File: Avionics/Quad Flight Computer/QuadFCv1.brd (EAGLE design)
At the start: 76.2 x 50.2 mm, 86 parts, among them J1 10104111_MICROUSBAB, SW1 2-1437565-9, U1 74LVC4245APW, U10 ATMEGA32U2-MU, U2 TM4C123GH6PZ, U3 MPU-6050-1, U4 HMC5883LSMD, U8 SPI_PPM, X3 HWB, Y1 32.768KHZ, Y2 AWSCR-20.00CW-T, Y3 PRQC16.00SR5010X000

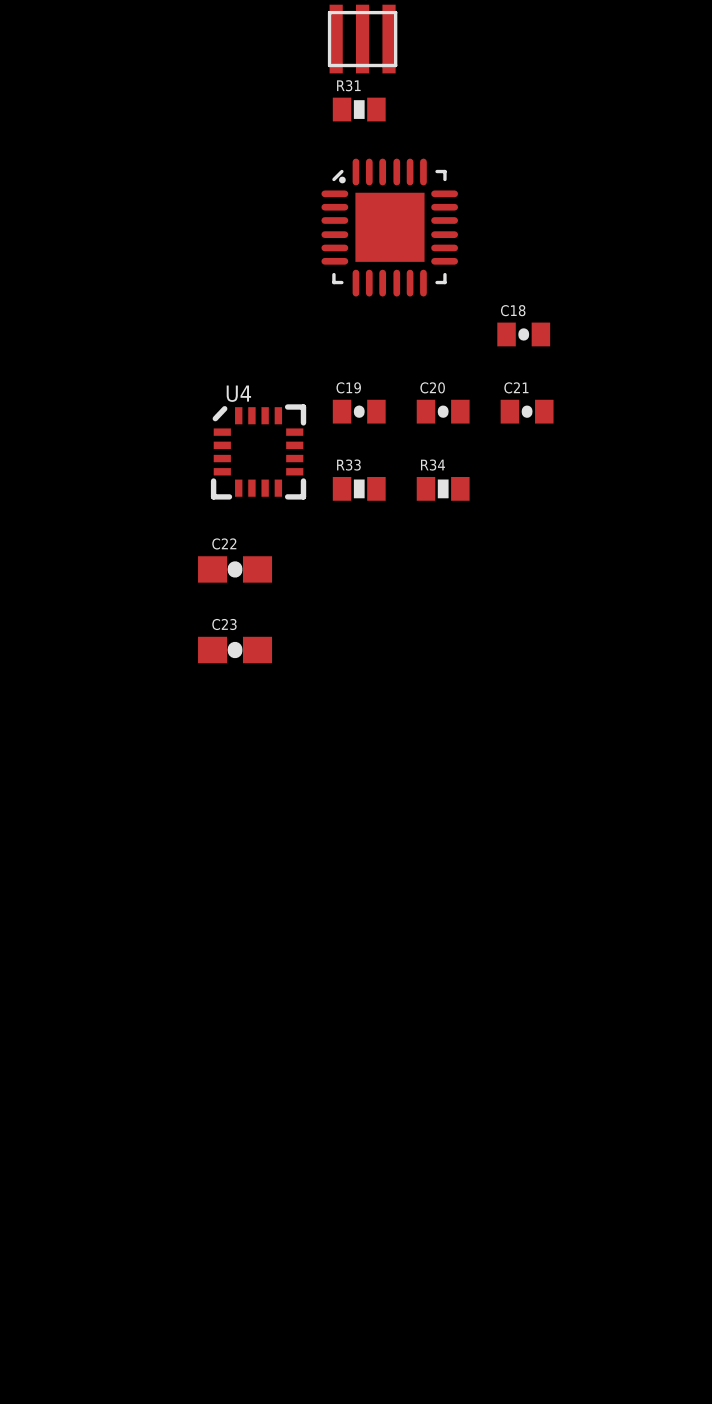
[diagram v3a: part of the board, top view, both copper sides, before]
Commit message: Exported all parts to libraries. Replaced IMU with MPU-6000.
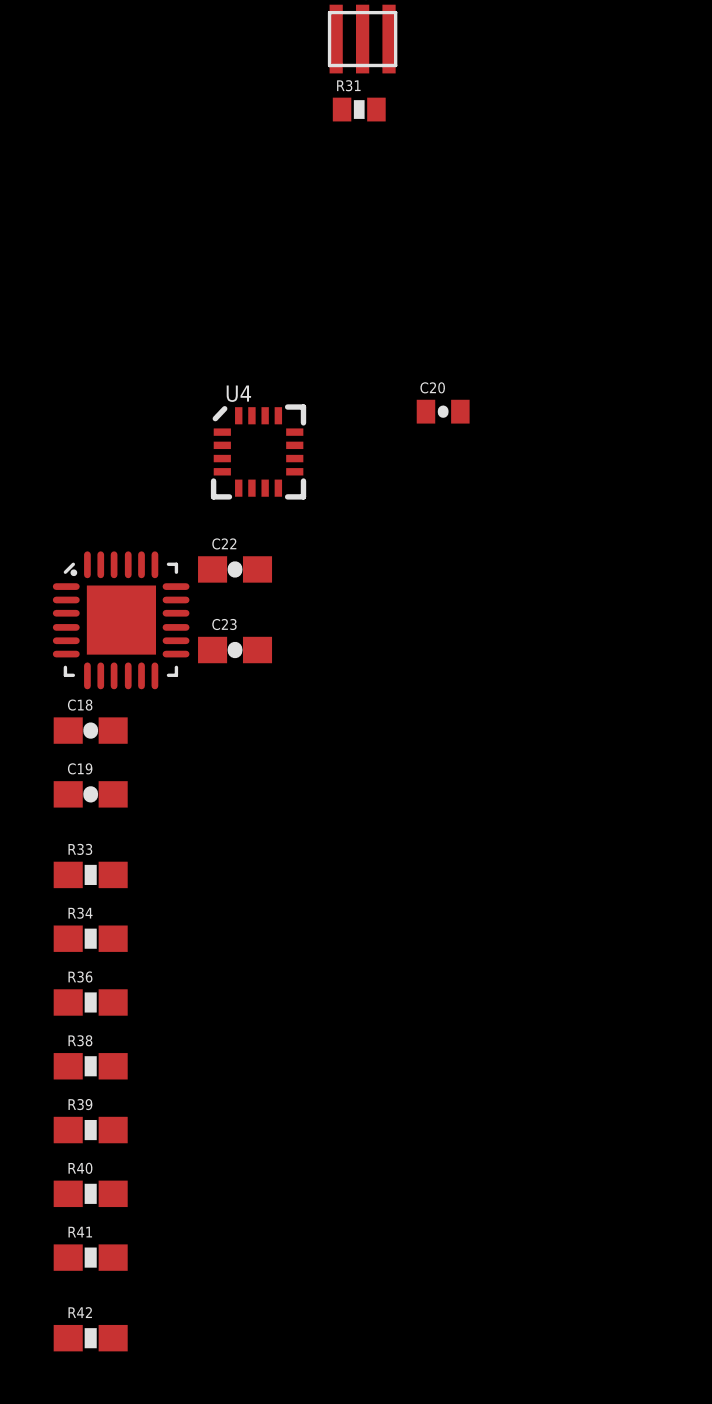
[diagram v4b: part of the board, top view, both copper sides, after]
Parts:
- removed C21: 10nF, SparkFun:0402-CAP
- removed U3: MPU-6050-1, Testing:QFN-24-4MM2
- added R36, R39, R40, R42: DNP, SparkFun-Resistors:0603-RES
- added R38, R41: 0, SparkFun-Resistors:0603-RES
- added U5: MPU-6000, Invesense:QFN-24-4MM2
- C18, C19: device SparkFun:0402-CAP -> SparkFun-Capacitors:0603-CAP
- R33, R34: value 10k -> 0; device SparkFun:0402-RES -> SparkFun-Resistors:0603-RES
- moved C18 22.2 mm to (-28.4, -177.3)
- moved R34 21.6 mm to (-28.4, -185.2)
- moved R33 17.8 mm to (-28.4, -182.8)
- moved C19 17.7 mm to (-28.4, -179.7)
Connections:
- removed net IMU_INT: U3.12
- removed net VIO: C21.1, U3.8
- new net FC_IMU_INT: U5.12
- new net FC_IMU_SPI_CS: R41.2
- new net FC_IMU_SPI_MISO: R38.1
- new net FC_IMU_SPI_MOSI: R34.2
- new net FC_IMU_SPI_SCLK: R33.2
- new net N$38: R33.1, R39.2, U5.23
- new net N$39: R34.1, R40.2, U5.24
- new net N$40: R41.1, U5.8
- new net N$41: R36.2, R38.2, R42.1, U5.9
- net 3.3V: now also R42.2, U5.13; no longer R33.2, R34.2, U3.13
- net AUX_SCL: now also U5.7; no longer U3.7
- net AUX_SDA: now also U5.6; no longer U3.6
- net FC_IMU_SCL: now also R39.1; no longer R33.1, U3.23
- net FC_IMU_SDA: now also R40.1; no longer R34.1, U3.24
- net GND: now also R36.1, U5.1, U5.11, U5.18; no longer C21.2, U3.1, U3.11, U3.18, U3.9
- net N$33: now also U5.20; no longer U3.20
- net N$34: now also U5.10; no longer U3.10

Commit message: Connected sensor network and added pressure sensor
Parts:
- removed R36, R42: DNP, SparkFun-Resistors:0603-RES
- removed R38, R41: 0, SparkFun-Resistors:0603-RES
- added C21: 0.1uF, SparkFun-Capacitors:0603-CAP
- added U6: MS5611-01BA, 3DRobotics:MS5611-01BA
- moved R33 30.5 mm to (-28.4, -213.2)
- moved R34 30.5 mm to (-28.4, -215.6)
- moved SW1 1.53 mm to (18.2, 34.5)
- moved J1 0.28 mm to (27.1, 4.83)
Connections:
- net PPM_STATUS0 renamed FC_PPM_STATUS0
- net PPM_STATUS1 renamed FC_PPM_STATUS1
- removed net FC_IMU_SCL: R39.1, U2.62, U4.1
- removed net FC_IMU_SDA: R40.1, U2.61, U4.16
- removed net FC_IMU_SPI_CS: R41.2
- removed net FC_IMU_SPI_MISO: R38.1
- removed net FC_IMU_SPI_MOSI: R34.2
- removed net FC_IMU_SPI_SCLK: R33.2
- removed net FC_SSI3CLK: U2.49
- removed net FC_SSI3FSS: U2.48
- removed net FC_SSI3RX: U2.47
- removed net FC_SSI3TX: U2.46
- removed net N$38: R33.1, R39.2, U5.23
- removed net N$39: R34.1, R40.2, U5.24
- removed net N$40: R41.1, U5.8
- removed net N$41: R36.2, R38.2, R42.1, U5.9
- new net FC_IMU_CS_L: U2.48, U5.8
- new net FC_IMU_MISO: U2.47, U5.9
- new net FC_IMU_MOSI: U2.46, U5.24
- new net FC_IMU_SCLK: U2.49, U5.23
- new net FC_PPM_IN: R28.1
- new net FC_SENSE_SCL: R33.2, U2.62, U6.8
- new net FC_SENSE_SDA: R34.2, U2.61, U6.7
- new net FC_USB_STATUS: R31.1
- new net MAG_SCL: R33.1, R39.1, U4.1
- new net MAG_SDA: R34.1, R40.1, U4.16
- net 3.3V: now also C21.1, U6.1, U6.2; no longer R42.2
- net AUX_SCL: now also R39.2
- net AUX_SDA: now also R40.2
- net GND: now also C21.2, U6.3, U6.5; no longer R36.1

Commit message: Added 16MB flash chip for core event logging and mission profile configuration. Internal EEPROM will be used for core configuration (failsafe modes, dead zones, etc), external flash will store mission parameters and user settings.
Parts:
- removed R46, R47, R51: 1k, SparkFun:0402-RES
- added R36: 1k, SparkFun:0402-RES
- added R38: DNP, SparkFun-Resistors:0603-RES
- added R41: 0, SparkFun-Resistors:0603-RES
- added U7: MS5611-01BA, 3DRobotics:MS5611-01BA
- added U9: S25FL127S, Shared Libraries:SOIC8
- C1: value 1uF -> 0.1uF; device SparkFun-Passives:0603-CAP -> SparkFun-Capacitors:0603-CAP
- C12: value 18pF -> 1uF
- C14: value .1uF -> 1uF; device SparkFun:0402-CAP -> SparkFun-Passives:0603-CAP
- C15: value 0.1uF -> .1uF; device SparkFun-Capacitors:0603-CAP -> SparkFun:0402-CAP
- C16: value .1uF -> 1uF
- C17: value 1uF -> .1uF
- C18: device SparkFun-Capacitors:0603-CAP -> SparkFun:0402-CAP
- C19: value 2.2nF -> 0.1uF
- C2, C3: value 1uF -> 0.1uF
- C20: value 0.1uF -> 2.2nF; device SparkFun:0402-CAP -> SparkFun-Capacitors:0603-CAP
- C21: value 0.1uF -> 4.7uF
- C23: value 4.7uF -> 0.1uF
- C7: value 0.1uF -> 18pF
- C9: value 0.1uF -> 1uF
- R13: value 0 -> 220; device SparkFun-Resistors:0805 -> SparkFun-Resistors:0603-RES
- R22: value 10K -> 220
- R23: value 49.9K -> 220
- R24: value 22 -> 220; device Shared Libraries:0603-RES -> SparkFun-Resistors:0603-RES
- R25: value 22-DNP -> 220; device Shared Libraries:0603-RES -> SparkFun-Resistors:0603-RES
- R26: value 22-DNP -> 49.9K; device Shared Libraries:0603-RES -> SparkFun-Resistors:0603-RES
- R27: value 0 -> 10K; device Shared Libraries:0603-RES -> SparkFun-Resistors:0603-RES
- R28: value 1K -> 1M
- R29: value 1M -> 10K
- R3: value 22 -> 22-DNP
- R31: value 1k -> 1K
- R33, R34: value 0 -> 1k; device SparkFun-Resistors:0603-RES -> SparkFun:0402-RES
- R37: value 10K -> 1k
- R4: value 0 -> 22; device SparkFun-Resistors:0805 -> Shared Libraries:0603-RES
- R40: value DNP -> 0
- R5: value 220 -> 22-DNP; device SparkFun-Resistors:0603-RES -> Shared Libraries:0603-RES
- R6: value 220 -> 0; device SparkFun-Resistors:0603-RES -> Shared Libraries:0603-RES
- R7: value 220 -> 22; device SparkFun-Resistors:0603-RES -> Shared Libraries:0603-RES
- R8, R9: value 220 -> 0; device SparkFun-Resistors:0603-RES -> SparkFun-Resistors:0805
- U1: value 74LVC4245APW -> TM4C123GH6PZ; device Shared Libraries:TSSOP24 -> Shared Libraries:LQFP100
- U2: value TM4C123GH6PZ -> 74LVC4245APW; device Shared Libraries:LQFP100 -> Shared Libraries:TSSOP24
- U4: value HMC5883LSMD -> SPI_PPM; device Shared Libraries:16LPCC -> SparkFunv2:2X3-NS
- U6: value MS5611-01BA -> HMC5883LSMD; device 3DRobotics:MS5611-01BA -> Shared Libraries:16LPCC
- U8: value SPI_PPM -> 74AUP1G19GW; device SparkFunv2:2X3-NS -> Shared Libraries:SOT363_PHILIPS
- moved C15 173.3 mm to (-4.95, -135.8), turned to 0 degrees
- moved C14 139.3 mm to (13.3, 1.91)
- moved C7 129.2 mm to (36.8, 26.0), turned to 270 degrees
- moved C4 128.6 mm to (39.4, 31.8), turned to 270 degrees
- moved C12 114.5 mm to (-18.4, -77.5), turned to 0 degrees
- moved U8 111.7 mm to (-28.3, -220.5)
- moved C1 106.4 mm to (-18.4, -99.7)
- moved R34 77.6 mm to (-15.1, -139.2)
- moved R33 77.5 mm to (-5.59, -139.2)
- moved JP1 73.3 mm to (73.0, 8.26), turned to 90 degrees
- moved JP2 73.3 mm to (3.81, 32.4), turned to 270 degrees
- moved R21 62.2 mm to (7.62, 19.7), turned to 180 degrees
- moved R12 62.1 mm to (69.2, 19.1), turned to 0 degrees
- moved R8 61.9 mm to (69.2, 13.3)
- moved R20 61.8 mm to (7.62, 21.8), turned to 180 degrees
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- renumbered F2 to F1, LED4 to LED2, LED5 to LED1, LED7 to LED3, U10 to U3, X3 to X1
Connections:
- removed net FC_SSI0CLK: U2.28
- removed net FC_SSI0FSS: U2.29
- removed net FC_SSI0RX: U2.30
- removed net FC_SSI0TX: U2.31
- new net FC_MEM_CLK: U1.28, U9.6
- new net FC_MEM_FSS: U1.29, U8.3
- new net FC_MEM_MISO: U1.30, U9.2
- new net FC_MEM_MOSI: U1.31, U9.5
- new net FC_MEM_SEL: U8.1
- new net FLASH_CS_L: U8.6, U9.1
- new net SD_CS_L: U8.4
- net 3.3V: now also C1.1, C13.1, C18.1, C2.1, C23.1, R26.2, U1.20, U1.32, U1.44, U1.5, U1.55, U1.56, U1.67, U1.7, U1.80, U1.93, U2.23, U2.24, U6.13, U6.4, U7.1, U7.2, U8.5, U9.8; no longer C20.1, C21.1, C4.1, C7.1, C9.1, R23.2, U1.23, U1.24, U2.20, U2.32, U2.44, U2.5, U2.55, U2.56, U2.67, U2.7, U2.80, U2.93, U4.13, U4.2, U4.4, U6.1
- net 5V: now also C15.1, C17.1, R29.2, R33.1, R34.1, R8.2, R9.2, U2.1, U4.2; no longer C14.1, C16.1, R13.2, R32.1, R37.2, R4.2, R51.1, U1.1, U8.2
- net AUX_SCL: now also R38.2; no longer R39.2
- net AUX_SDA: now also R39.2; no longer R40.2
- net FC_AIN0: now also U1.12; no longer U2.12
- net FC_AIN1: now also U1.13; no longer U2.13
- net FC_AIN20: now also U1.90; no longer U2.90
- net FC_AIN21: now also U1.89; no longer U2.89
- net FC_AIN4: now also U1.100; no longer U2.100
- net FC_AIN5: now also U1.99; no longer U2.99
- net FC_IMU_CS_L: now also U1.48; no longer U2.48
- net FC_IMU_MISO: now also U1.47; no longer U2.47
- net FC_IMU_MOSI: now also U1.46; no longer U2.46
- net FC_IMU_SCLK: now also U1.49; no longer U2.49
- net FC_JTAG_TCK: now also U1.85; no longer U2.85
- net FC_JTAG_TDI: now also U1.83; no longer U2.83
- net FC_JTAG_TDO: now also U1.82; no longer U2.82
- net FC_JTAG_TMS: now also U1.84; no longer U2.84
- net FC_MAG_DRDY_L: now also U6.15; no longer U4.15
- net FC_PA6: now also U1.34; no longer U2.34
- net FC_PA7: now also U1.35; no longer U2.35
- net FC_PB2: now also U1.72; no longer U2.72
- net FC_PB3: now also U1.73; no longer U2.73
- net FC_PB4: now also U1.92; no longer U2.92
- net FC_PB5: now also U1.91; no longer U2.91
- net FC_PD0: now also U1.1; no longer U2.1
- net FC_PD1: now also U1.2; no longer U2.2
- net FC_PD2: now also U1.3; no longer U2.3
- net FC_PD3: now also U1.4; no longer U2.4
- net FC_PD4: now also U1.97; no longer U2.97
- net FC_PD5: now also U1.98; no longer U2.98
- net FC_PE4: now also U1.95; no longer U2.95
- net FC_PE5: now also U1.96; no longer U2.96
- net FC_PF0: now also U1.40; no longer U2.40
- net FC_PF1: now also U1.41; no longer U2.41
- net FC_PF2: now also U1.42; no longer U2.42
- net FC_PF3: now also U1.43; no longer U2.43
- net FC_PF4: now also U1.39; no longer U2.39
- net FC_PF5: now also U1.37; no longer U2.37
- net FC_PF6: now also U1.36; no longer U2.36
- net FC_PF7: now also U1.58; no longer U2.58
- net FC_PG2: now also U1.60; no longer U2.60
- net FC_PG3: now also U1.59; no longer U2.59
- net FC_PG4: now also U1.74; no longer U2.74
- net FC_PG5: now also U1.75; no longer U2.75
- net FC_PG6: now also U1.87; no longer U2.87
- net FC_PG7: now also U1.88; no longer U2.88
- net FC_PJ2: now also U1.11; no longer U2.11
- net FC_PPM_IN: now also R31.1; no longer R28.1
- net FC_PPM_STATUS0: now also R37.1; no longer R47.1
- net FC_PPM_STATUS1: now also R32.1; no longer R46.1
- net FC_PWMOUT1: now also U1.16, U2.21; no longer U1.21, U2.16
- net FC_PWMOUT2: now also U1.17, U2.20; no longer U1.20, U2.17
- net FC_PWMOUT3: now also U1.18, U2.19; no longer U1.19, U2.18
- net FC_PWMOUT4: now also U1.19, U2.18; no longer U1.18, U2.19
- net FC_PWMOUT5: now also U1.79, U2.17; no longer U1.17, U2.79
- net FC_PWMOUT6: now also U1.78, U2.16; no longer U1.16, U2.78
- net FC_PWMOUT7: now also U1.77, U2.15; no longer U1.15, U2.77
- net FC_PWMOUT8: now also U1.76, U2.14; no longer U1.14, U2.76
- net FC_PWMOUT_ARM_L: now also R26.1, U2.22; no longer R23.1, U1.22
- net FC_RESET_L: now also C4.1, U1.63; no longer C15.1, U2.63
- net FC_SENSE_SCL: now also R41.2, U1.62, U7.8; no longer R33.2, U2.62, U6.8
- net FC_SENSE_SDA: now also R40.2, U1.61, U7.7; no longer R34.2, U2.61, U6.7
- net FC_U0RX: now also U1.26; no longer U2.26
- net FC_U0TX: now also U1.27; no longer U2.27
- net FC_U1RX: now also U1.25; no longer U2.25
- net FC_U1TX: now also U1.24; no longer U2.24
- net FC_U3RX: now also U1.23; no longer U2.23
- net FC_U3TX: now also U1.22; no longer U2.22
- net FC_U7RX: now also U1.15; no longer U2.15
- net FC_U7TX: now also U1.14; no longer U2.14
- net FC_USB0DM: now also R7.1, U1.68; no longer R3.1, U2.68
- net FC_USB0DP: now also R4.1, U1.69; no longer R24.1, U2.69
- net FC_USB0ID: now also R6.1, U1.70; no longer R27.1, U2.70
- net FC_USB0VBUS: now also U1.71; no longer U2.71
- net FC_USB_STATUS: now also R36.1; no longer R31.1
- net GND: now also C1.2, C12.2, C14.1, R27.1, U1.10, U1.21, U1.33, U1.45, U1.57, U1.6, U1.64, U1.81, U1.9, U1.94, U2.11, U2.12, U2.13, U4.6, U6.11, U6.9, U7.3, U7.5, U8.2, U9.4; no longer C1.1, C14.2, C7.2, R22.1, U1.11, U1.12, U1.13, U2.10, U2.21, U2.33, U2.45, U2.57, U2.6, U2.64, U2.81, U2.9, U2.94, U4.11, U4.9, U6.3, U6.5, U8.6
- net GNDX: now also C7.2, U1.53; no longer C12.2, U2.53
- net MAG_SCL: now also R38.1, R41.1, U6.1; no longer R33.1, R39.1, U4.1
- net MAG_SDA: now also R39.1, U6.16; no longer R34.1, U4.16
- net N$1: now also JP2.3, R18.2; no longer JP1.3, R5.2
- net N$10: now also JP1.4, R11.2; no longer JP2.4, R15.2
- net N$11: now also JP1.5, R12.2; no longer JP2.5, R16.2
- net N$12: now also JP1.6, R13.2; no longer JP2.6, R17.2
- net N$13: now also JP1.7, R14.2; no longer JP2.7, R18.2
- net N$14: now also JP1.8, R15.2; no longer JP2.8, R19.2
- net N$15: now also JP1.9, R16.2; no longer JP2.9, R20.2
- net N$16: now also JP1.10, R17.2; no longer JP2.10, R21.2
- net N$17: now also C14.2, U1.8; no longer C1.2, U2.8
- net N$18: now also C12.1, C9.1, U1.38, U1.86; no longer C13.1, C2.1, U2.38, U2.86
- net N$19: now also C11.1, U1.54; no longer C12.1, U2.54
- net N$2: now also JP2.4, R19.2; no longer JP1.4, R6.2
- net N$20: now also R27.2, U2.2; no longer R22.2, U1.2
- net N$21: now also C7.1, U1.52; no longer C11.1, U2.52
- net N$22: now also U1.50; no longer U2.50
- net N$23: now also JP2.2, R9.1; no longer JP1.2, R4.1
- net N$24: now also U1.65; no longer U2.65
- net N$25: now also U1.66; no longer U2.66
- net N$26: now also JP1.2, R8.1; no longer JP2.2, R13.1
- net N$27: now also R6.2; no longer R27.2
- net N$28: now also R7.2; no longer R26.2
- net N$29: now also R4.2, R5.2; no longer R24.2, R25.2
- net N$3: now also JP2.5, R20.2; no longer JP1.5, R7.2
- net N$30: now also R33.2; no longer R35.2
- net N$31: now also R34.2; no longer R32.2
- net N$32: now also R35.2; no longer R51.2
- net N$33: now also C20.1; no longer C19.1
- net N$34: now also C19.1; no longer C18.1
- net N$35: now also C21.1, U6.10; no longer C23.1, U4.10
- net N$36: now also U6.8; no longer U4.8
- net N$37: now also U6.12; no longer U4.12
- net N$4: now also JP2.6, R21.2; no longer JP1.6, R8.2
- net N$5: now also JP2.7, R22.2; no longer JP1.7, R9.2
- net N$6: now also JP2.8, R23.2; no longer JP1.8, R10.2
- net N$7: now also JP2.9, R24.2; no longer JP1.9, R11.2
- net N$8: now also JP2.10, R25.2; no longer JP1.10, R12.2
- net N$9: now also JP1.3, R10.2; no longer JP2.3, R14.2
- net PPM_OUT: now also R31.2; no longer R28.2
- net PPM_PD0: now also R37.2; no longer R47.2
- net PPM_PD1: now also R32.2; no longer R46.2
- net PPM_RST: now also R29.1, U4.5; no longer R37.1, U8.5
- net PPM_USBDM: now also R3.1; no longer R26.1
- net PPM_USBDP: now also R5.1; no longer R25.1
- net PPM_USB_STATUS: now also R36.2; no longer R31.2
- net PWMIN1: now also R18.1; no longer R5.1
- net PWMIN2: now also R19.1, U4.3; no longer R6.1, U8.3
- net PWMIN3: now also R20.1, U4.4; no longer R7.1, U8.4
- net PWMIN4: now also R21.1, U4.1; no longer R8.1, U8.1
- net PWMIN5: now also R22.1; no longer R9.1
- net PWMIN6: now also R23.1; no longer R10.1
- net PWMIN7: now also R24.1; no longer R11.1
- net PWMIN8: now also R25.1; no longer R12.1
- net PWMOUT1: now also R10.1, U2.3; no longer R14.1, U1.3
- net PWMOUT2: now also R11.1, U2.4; no longer R15.1, U1.4
- net PWMOUT3: now also R12.1, U2.5; no longer R16.1, U1.5
- net PWMOUT4: now also R13.1, U2.6; no longer R17.1, U1.6
- net PWMOUT5: now also R14.1, U2.7; no longer R18.1, U1.7
- net PWMOUT6: now also R15.1, U2.8; no longer R19.1, U1.8
- net PWMOUT7: now also R16.1, U2.9; no longer R20.1, U1.9
- net PWMOUT8: now also R17.1, U2.10; no longer R21.1, U1.10
- net VUCAP: now also C16.1; no longer C17.1
- net XT1: now also R28.2; no longer R29.2
- net XT2: now also R28.1; no longer R29.1

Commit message: Added Micro SD Card slot
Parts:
- added J2: 1050270001, Shared Libraries:1050270001
- added R42, R43: 2.2k, Shared Libraries:0603-RES
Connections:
- new net FC_SD_PRESENT: J2.G1
- net 3.3V: now also J2.P4, R42.2, R43.2
- net FC_MEM_CLK: now also J2.P5
- net FC_MEM_MISO: now also J2.P7
- net FC_MEM_MOSI: now also J2.P3
- net FC_SENSE_SCL: now also R42.1
- net FC_SENSE_SDA: now also R43.1
- net GND: now also J2.P6
- net SD_CS_L: now also J2.P2
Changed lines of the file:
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@@
 <element name="U8" library="Shared Libraries" package="SOT363_PHILIPS" value="74AUP1G19GW" x="-28.321" y="-220.472"/>
 <element name="U9" library="Shared Libraries" package="SOIC8" value="S25FL127S" x="-34.544" y="-219.837"/>
+<element name="R42" library="Shared Libraries" package="0603-RES" value="2.2k" x="-37.338" y="-225.044"/>
+<element name="R43" library="Shared Libraries" package="0603-RES" value="2.2k" x="-37.338" y="-227.457"/>
+<element name="J2" library="Shared Libraries" package="1050270001" value="1050270001" x="56.515" y="78.232"/>
 </elements>
 <signals>
@@
 <contactref element="U8" pad="5"/>
 <contactref element="U9" pad="8"/>
+<contactref element="R43" pad="2"/>
+<contactref element="R42" pad="2"/>
+<contactref element="J2" pad="P4"/>
+<wire x1="-36.488" y1="-225.044" x2="-36.449" y2="-217.237" width="0" layer="19" extent="1-1"/>
+<wire x1="-36.488" y1="-227.457" x2="-36.488" y2="-225.044" width="0" layer="19" extent="1-1"/>
+<wire x1="57.415" y1="71.572" x2="-36.449" y2="-217.237" width="0" layer="19" extent="1-1"/>
 <wire x1="-28.321" y1="-219.672" x2="-36.449" y2="-217.237" width="0" layer="19" extent="1-1"/>
 <wire x1="-29.298" y1="-210.82" x2="-28.321" y2="-219.672" width="0" layer="19" extent="1-1"/>
@@
 <contactref element="U8" pad="2"/>
 <contactref element="U9" pad="4"/>
+<contactref element="J2" pad="P6"/>
 <wire x1="-28.321" y1="-221.272" x2="-32.639" y2="-222.437" width="0" layer="19" extent="1-1"/>
 <wire x1="-27.598" y1="-210.82" x2="-28.321" y2="-221.272" width="0" layer="19" extent="1-1"/>
 <wire x1="-26.332" y1="-207.361" x2="-27.598" y2="-210.82" width="0" layer="19" extent="1-1"/>
 <wire x1="-28.532" y1="-206.111" x2="-26.332" y2="-207.361" width="0" layer="19" extent="1-1"/>
+<wire x1="54.865" y1="71.572" x2="-32.639" y2="-222.437" width="0" layer="19" extent="1-1"/>
 <wire x1="-27.598" y1="-179.705" x2="-28.532" y2="-206.111" width="0" layer="19" extent="1-1"/>
 <wire x1="-27.598" y1="-177.292" x2="-27.598" y2="-179.705" width="0" layer="19" extent="1-1"/>
@@
 <contactref element="U1" pad="28"/>
 <contactref element="U9" pad="6"/>
+<contactref element="J2" pad="P5"/>
+<wire x1="55.965" y1="71.572" x2="-33.909" y2="-217.237" width="0" layer="19" extent="1-1"/>
 <wire x1="52.625" y1="26.135" x2="-33.909" y2="-217.237" width="0" layer="19" extent="1-1"/>
 </signal>
@@
 <contactref element="U1" pad="30"/>
 <contactref element="U9" pad="2"/>
+<contactref element="J2" pad="P7"/>
 <wire x1="-35.179" y1="-222.437" x2="51.625" y2="26.135" width="0" layer="19" extent="1-1"/>
+<wire x1="53.765" y1="71.572" x2="-35.179" y2="-222.437" width="0" layer="19" extent="1-1"/>
 </signal>
 <signal name="FC_MEM_MOSI">
 <contactref element="U1" pad="31"/>
 <contactref element="U9" pad="5"/>
+<contactref element="J2" pad="P3"/>
+<wire x1="58.165" y1="71.572" x2="-32.639" y2="-217.237" width="0" layer="19" extent="1-1"/>
 <wire x1="51.125" y1="26.135" x2="-32.639" y2="-217.237" width="0" layer="19" extent="1-1"/>
 </signal>
@@
 <contactref element="U1" pad="62"/>
 <contactref element="U7" pad="8"/>
+<contactref element="R42" pad="1"/>
 <wire x1="-26.332" y1="-203.611" x2="-27.598" y2="-213.233" width="0" layer="19" extent="1-1"/>
+<wire x1="-38.188" y1="-225.044" x2="-27.598" y2="-213.233" width="0" layer="19" extent="1-1"/>
 <wire x1="39.905" y1="18.915" x2="-26.332" y2="-203.611" width="0" layer="19" extent="1-1"/>
 </signal>
@@
 <contactref element="U7" pad="7"/>
 <contactref element="R40" pad="2"/>
+<contactref element="R43" pad="1"/>
 <wire x1="-26.332" y1="-204.861" x2="-27.598" y2="-215.646" width="0" layer="19" extent="1-1"/>
+<wire x1="-38.188" y1="-227.457" x2="-27.598" y2="-215.646" width="0" layer="19" extent="1-1"/>
 <wire x1="39.905" y1="19.415" x2="-26.332" y2="-204.861" width="0" layer="19" extent="1-1"/>
 </signal>
@@
 <signal name="SD_CS_L">
 <contactref element="U8" pad="4"/>
+<contactref element="J2" pad="P2"/>
+<wire x1="59.265" y1="71.572" x2="-27.671" y2="-219.672" width="0" layer="19" extent="1-1"/>
+</signal>
+<signal name="FC_SD_PRESENT">
+<contactref element="J2" pad="G1"/>
 </signal>
 </signals>

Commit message: Added several connectors and modified power inputs to not immediately go to 5V plane.
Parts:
- added FC_JTAG: M04X2, SparkFun-Connectors:2X4
- added GPS, I2C: (no value), Shared Libraries:DF13_4POS
- added JP3: (no value), Shared Libraries:DF13_5POS
- added R44: 120K, Shared Libraries:0603-RES
- added R45: 20K, Shared Libraries:0603-RES
- added R46, R47, R48, R49, R50, R51: 10k, Shared Libraries:0603-RES
- added R52: 0, Shared Libraries:0603-RES
- added R53: DNP, Shared Libraries:0603-RES
- added R54, R55: DNP, SparkFun-Resistors:0805
- added VBATT: M01PTH, SparkFun-Connectors:1X01
- C15, C16, C17, C18: device SparkFun:0402-CAP -> SparkFun:C0402
- R28, R29, R30, R31, R32, R33, R34, R35, R36, R37: device SparkFun:0402-RES -> SparkFun:C0402
- moved R43 319.4 mm to (99.7, 61.1), turned to 90 degrees
- moved R42 316.2 mm to (97.3, 61.1), turned to 90 degrees
- moved U8 314.8 mm to (92.7, 70.1), turned to 90 degrees
- moved R40 308.4 mm to (87.9, 70.0), turned to 90 degrees
- moved R41 305.3 mm to (85.5, 70.0), turned to 90 degrees
- moved C23 302.1 mm to (83.1, 70.0), turned to 90 degrees
- moved R39 281.5 mm to (67.1, 70.0), turned to 90 degrees
- moved U7 281.4 mm to (67.4, 59.4), turned to 90 degrees
- moved R38 278.4 mm to (64.6, 70.0), turned to 90 degrees
- moved C20 262.3 mm to (51.9, 70.0), turned to 90 degrees
- moved C19 259.3 mm to (49.5, 70.0), turned to 90 degrees
- moved C21 259.2 mm to (46.5, 75.4), turned to 90 degrees
- moved C22 255.4 mm to (43.4, 75.4), turned to 90 degrees
- moved U5 254.8 mm to (45.3, 71.1), turned to 90 degrees
- moved C18 254.0 mm to (37.5, 83.3), turned to 90 degrees
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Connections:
- new net 5VBATT: R55.2, R9.2
- new net EXT_I2C_SCL: I2C.P3
- new net EXT_I2C_SDA: I2C.P2
- new net GPS_RX: GPS.P3
- new net GPS_TX: GPS.P2
- new net ISENSE1: R48.2
- new net ISENSE2: R47.2
- new net ISENSE3: R51.2
- new net ISENSE4: R50.2
- new net ISENSE5V: R49.2
- new net N$38: R44.1, R45.2, R46.1
- new net N$39: GPS.P1, R52.1, R53.1
- new net N$44: JP3.P1, R51.1
- new net N$45: JP3.P2, R50.1
- new net N$46: JP3.P3, R49.1
- new net N$47: JP3.P4, R48.1
- new net N$48: JP3.P5, R47.1
- new net VBATT: R44.2, VBATT.1
- new net VBATTSENSE: R46.2
- net 3.3V: now also FC_JTAG.4, I2C.P1, R53.2
- net 5V: now also R52.2, R54.2; no longer R9.2
- net FC_JTAG_TCK: now also FC_JTAG.1
- net FC_JTAG_TDI: now also FC_JTAG.5
- net FC_JTAG_TDO: now also FC_JTAG.7
- net FC_JTAG_TMS: now also FC_JTAG.3
- net FC_RESET_L: now also FC_JTAG.2
- net GND: now also FC_JTAG.6, FC_JTAG.8, GPS.P4, I2C.P4, R45.1
- net N$23: now also R54.1
- net N$26: now also R55.1
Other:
- board size 76.2 x 50.2 mm -> 63.5 x 38.1 mm
